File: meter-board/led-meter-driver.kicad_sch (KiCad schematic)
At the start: 88 parts, among them U10 TLV1814RTER, U11 TLV1814RTER, U12 TLV1814RTER, U13 TLV1814RTER, U14 TLV1814RTER, U15 TLV1814RTER, U16 TBD62183AFNG,EL, U17 TBD62183AFNG,EL, U18 TBD62183AFNG,EL, U19 TBD62183AFNG,EL, U20 TLV1814RTER, U9 TLV1814RTER

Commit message: update circuits
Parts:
- added R153, R154, R155, R156: 100k, my_Resistor:R_0402_1005M, symbol my_Resistor:R_0402_1005M
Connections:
- net G5_AIN: now also R155.1
- net G6R6_AIN: now also R153.1
- net GND: now also R153.2, R154.2, R155.2, R156.2
- net R10_AIN: now also R156.1
- net R5_AIN: now also R154.1

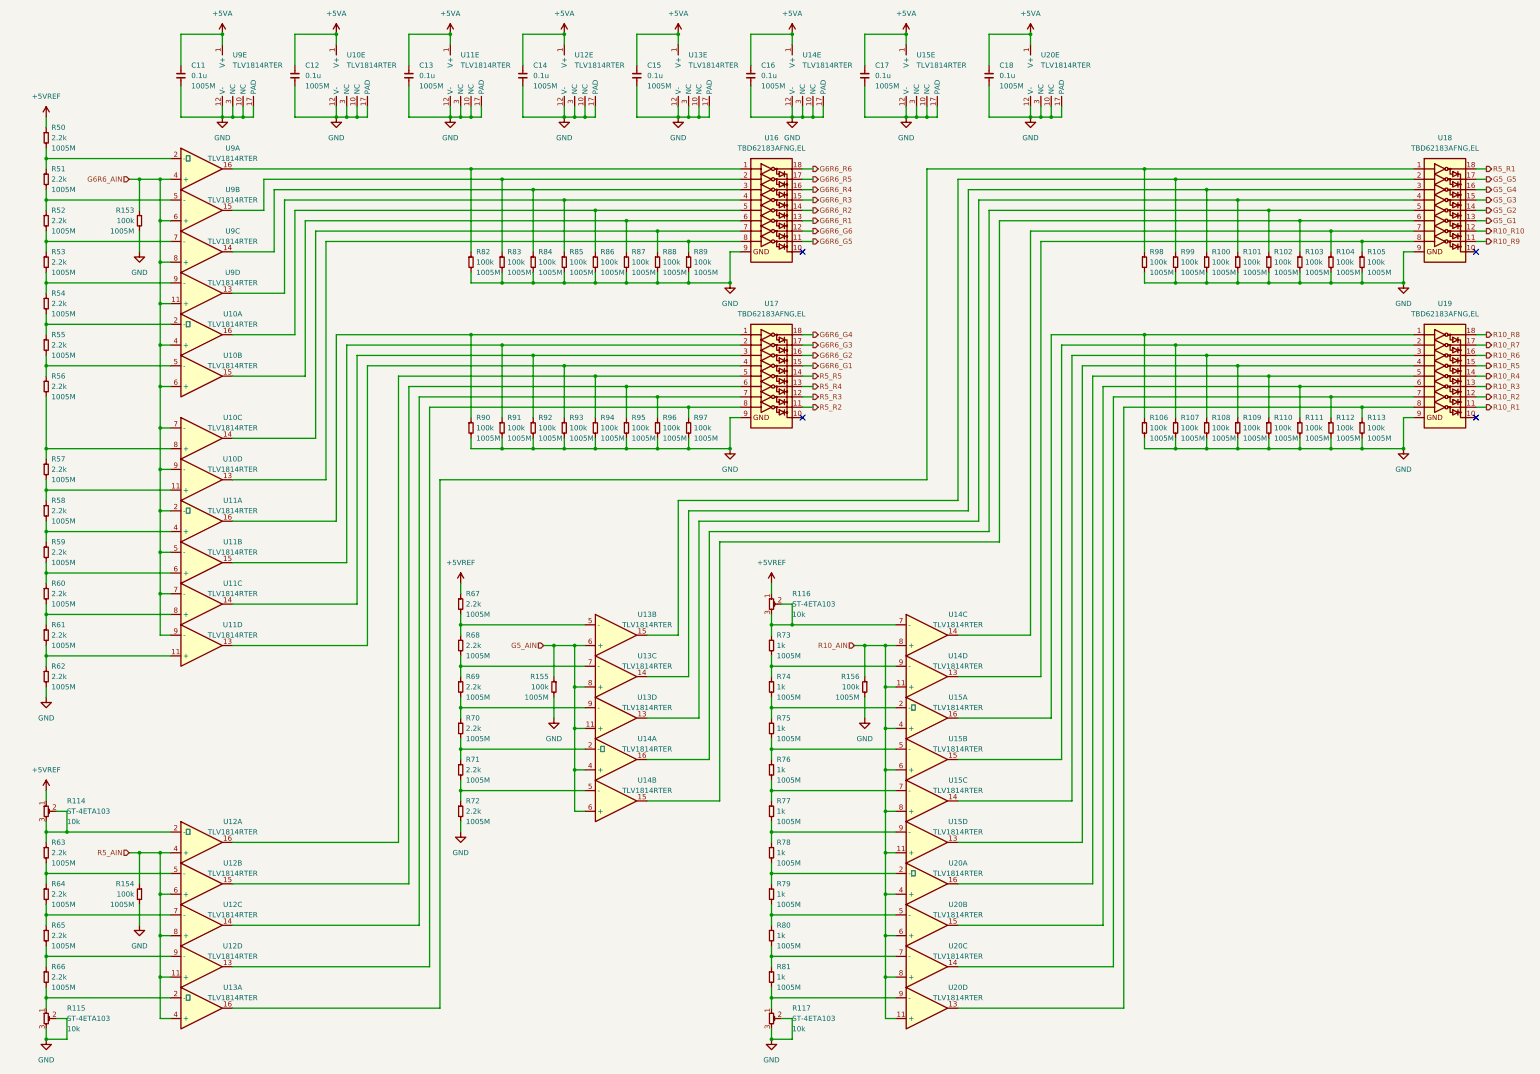
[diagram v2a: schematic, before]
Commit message: add input filter
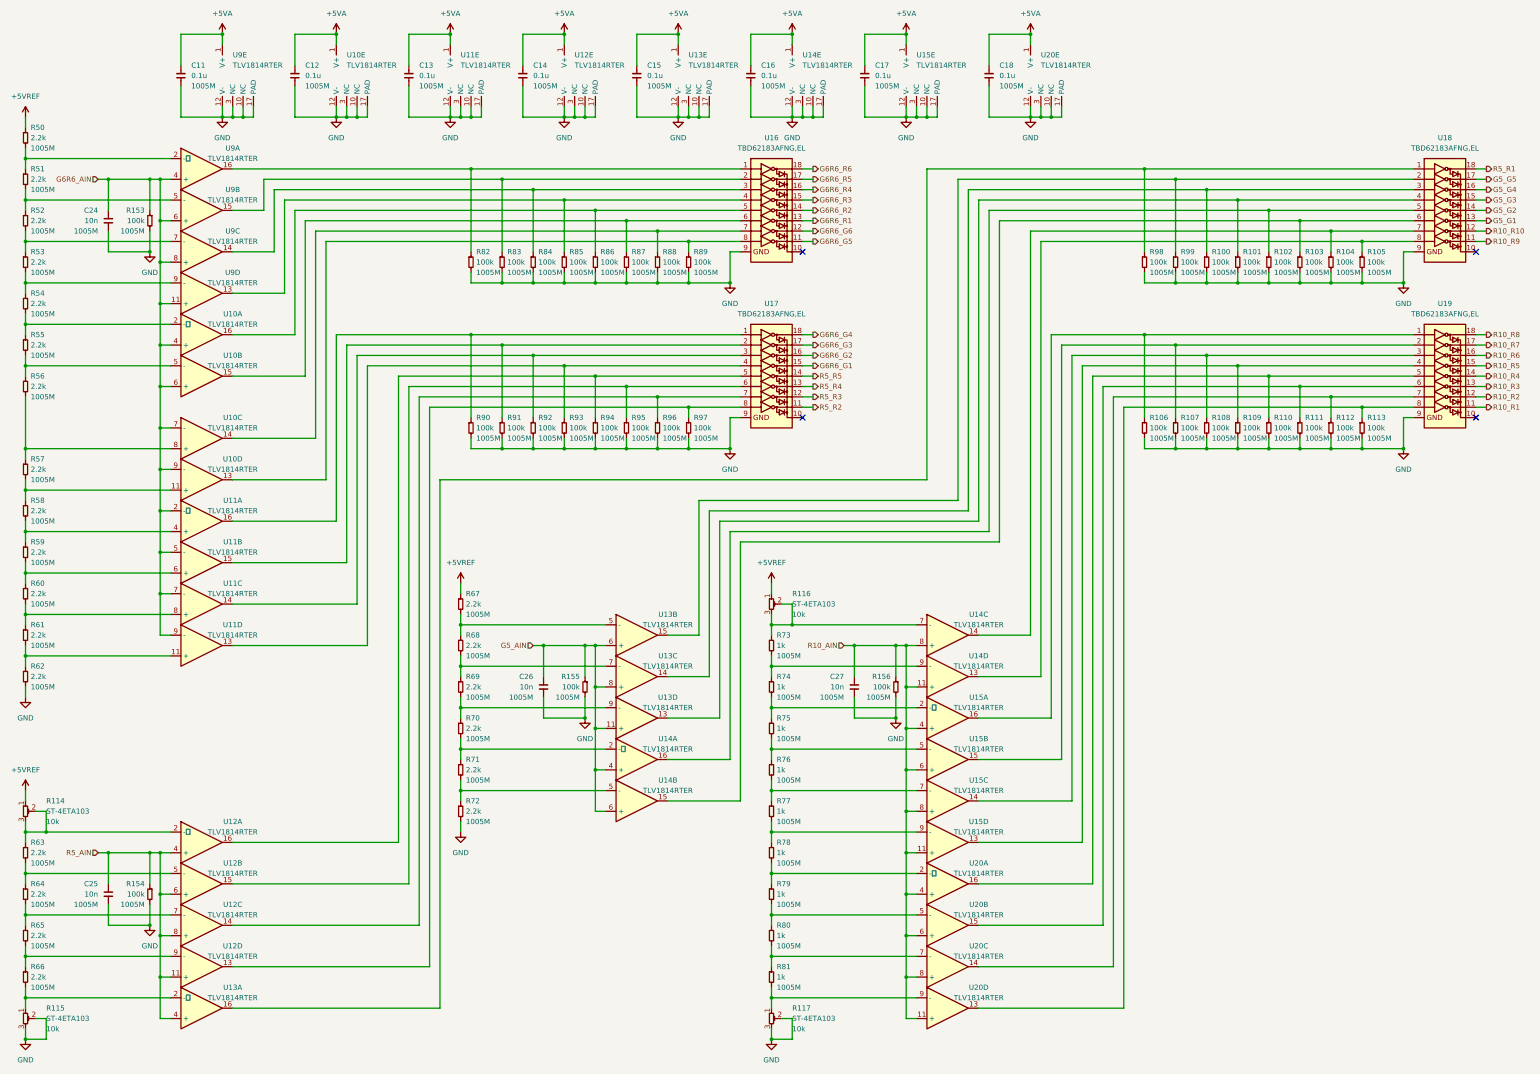
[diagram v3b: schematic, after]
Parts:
- added C24, C25, C26, C27: 10n, my_Capacitor:C_0402_1005M, symbol my_Capacitor:C_0402_1005M
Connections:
- net G5_AIN: now also C26.1
- net G6R6_AIN: now also C24.1
- net GND: now also C24.2, C25.2, C26.2, C27.2
- net R10_AIN: now also C27.1
- net R5_AIN: now also C25.1
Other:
- moved on the sheet: R114, R115, R153, R154, R155, R156, R50, R51, R52, R53, R54, R55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
